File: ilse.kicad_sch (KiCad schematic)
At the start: 89 parts, among them J1 OUT, J2 EURO RACK POWER, J3 CV Inputs, J4 1V/Oct, J5 Gate, J6 Cutoff, J7 Filter In, Q1 BC560, Q2 BC560, Q3 BC560, Q4 BC550, Q5 BC550, Q6 BC550, SW1 Power Switch, SW2 LFO to Filter / Freq CV, SW3 Resonance L/H, U1 TL074, U2 TL074

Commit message: choose volume pot as linear type
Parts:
- H1, H2, H3, H4, LOGO1: now left out of the parts list
- RV7: value 100kA -> 100kB

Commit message: incorporates max's powersupply protection
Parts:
- removed SW1: Power Switch, chair:PVA2, symbol CHAIR:SW_Push_DPDT-Switch-PVA2
- added D3, D4: 1N5819, Diode_THT:D_DO-41_SOD81_P10.16mm_Horizontal, symbol Diode:1N5819
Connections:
- net VCC: now also C12.1, D3.1 (K)
- net VSS: now also C13.2, D4.2 (A)
- net at BT1.1 (+), J2.1 (+12V), J2.2 (+12V): now also D3.2 (A); no longer C12.1
- net at BT2.2 (-), J2.10 (-12V), J2.9 (-12V): now also D4.1 (K); no longer C13.2

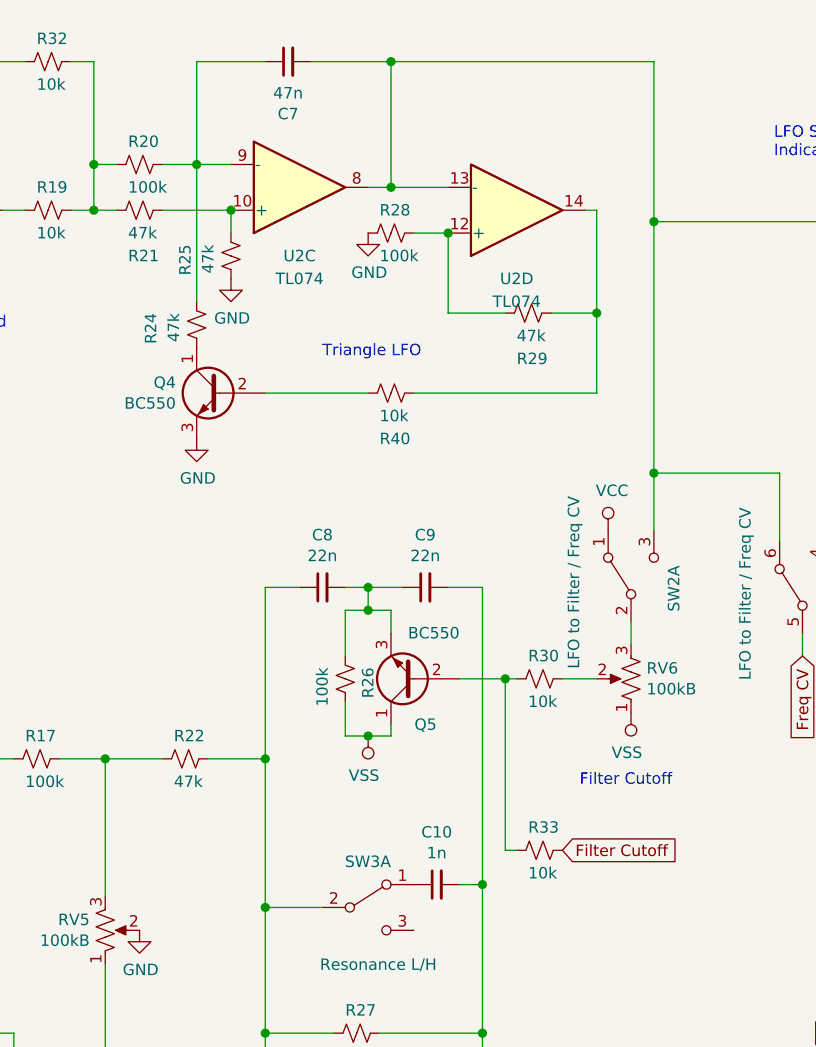
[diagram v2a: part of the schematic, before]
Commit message: removes filter distortion, cutoff modulation range is 0V - +10V, instead of -10V - +10V
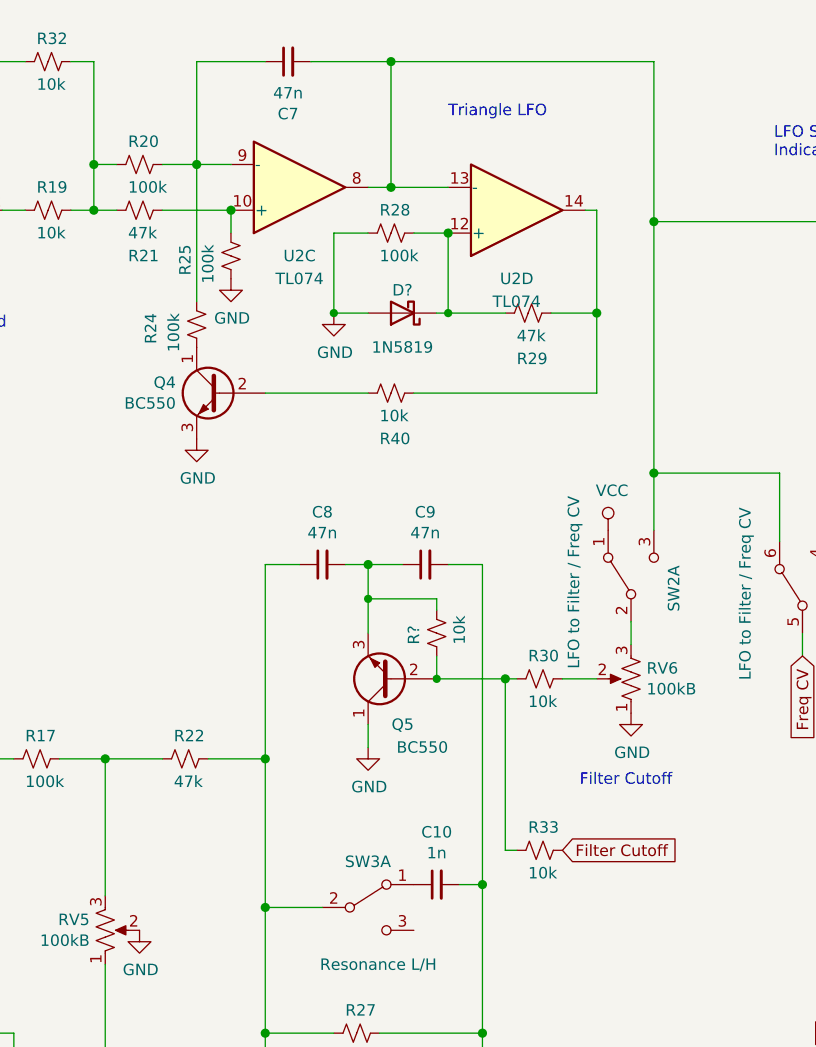
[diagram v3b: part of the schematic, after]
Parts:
- removed R26: 100k, Resistor_THT:R_Axial_DIN0207_L6.3mm_D2.5mm_P10.16mm_Horizontal, symbol ilse-rescue:R_Small_US-Device
- added D?: 1N5819, Diode_THT:D_DO-41_SOD81_P10.16mm_Horizontal, symbol Diode:1N5819
- added R?: 10k, Resistor_THT:R_Axial_DIN0207_L6.3mm_D2.5mm_P10.16mm_Horizontal, symbol ilse-rescue:R_Small_US-Device
- C8, C9: value 22n -> 47n
- R24, R25: value 47k -> 100k
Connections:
- net GND: now also Q5.1 (C), RV6.1, D?.2 (A)
- net VSS: no longer Q5.1 (C), RV6.1
- net at C8.2, C9.1, Q5.3 (E): now also R?.1
- net at Q5.2 (B), R30.2, R33.2: now also R?.2
- net at R28.1, R29.2, U2.12 (+): now also D?.1 (K)
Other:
- moved on the sheet: C8, C9, Q5

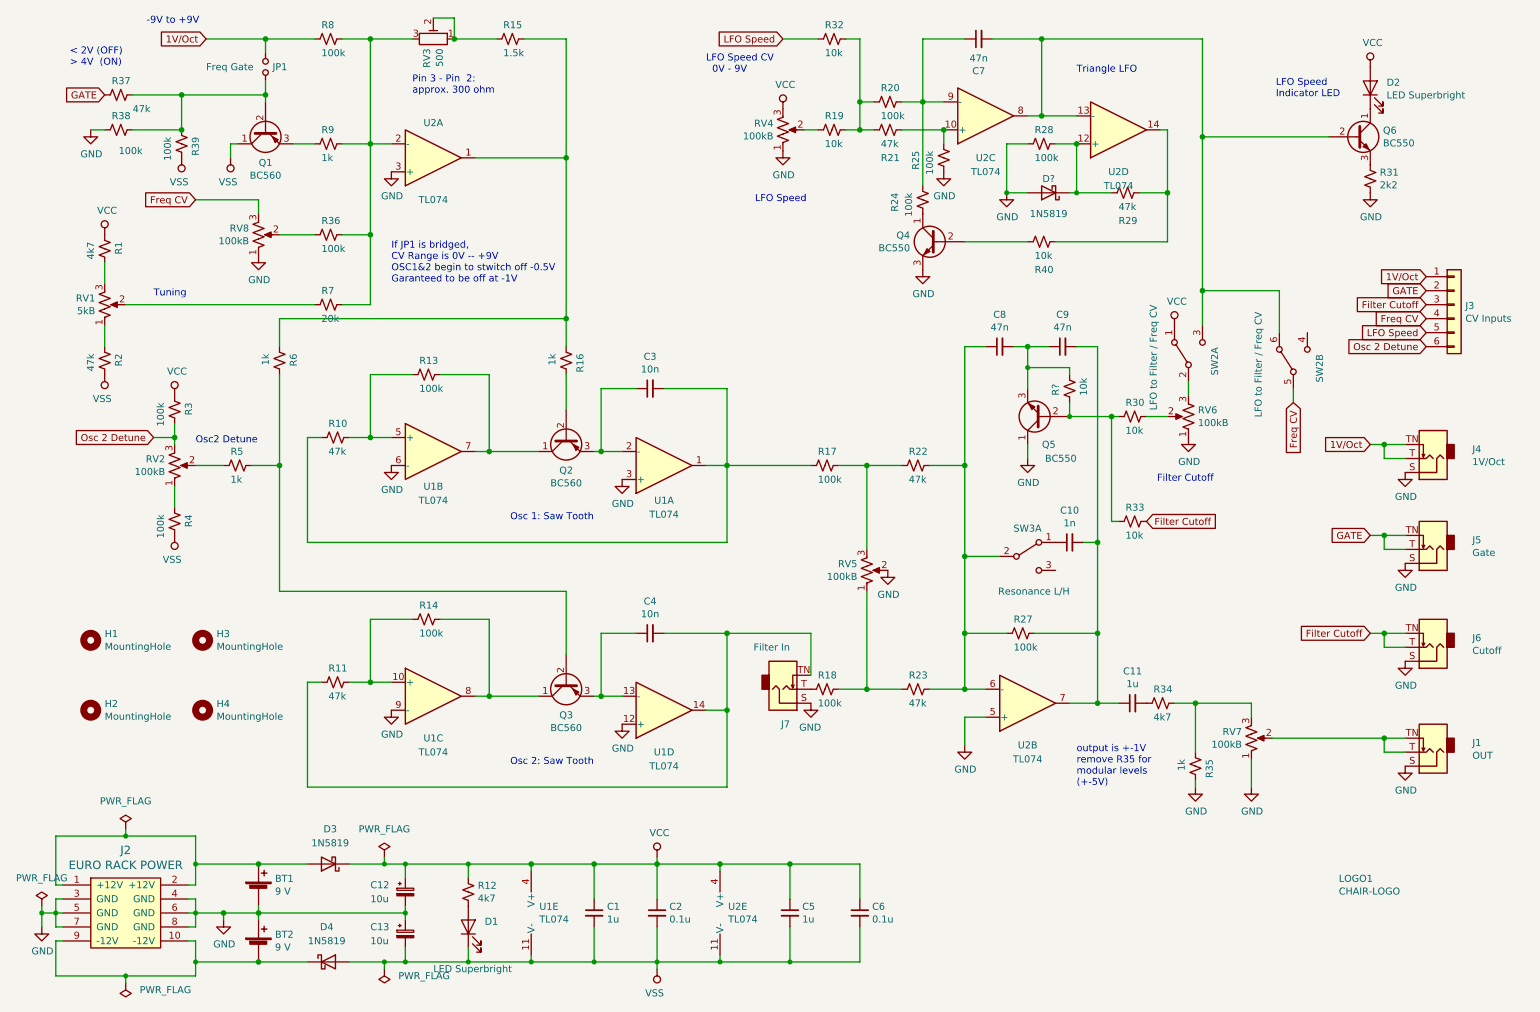
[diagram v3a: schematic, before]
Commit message: added hybrid lib
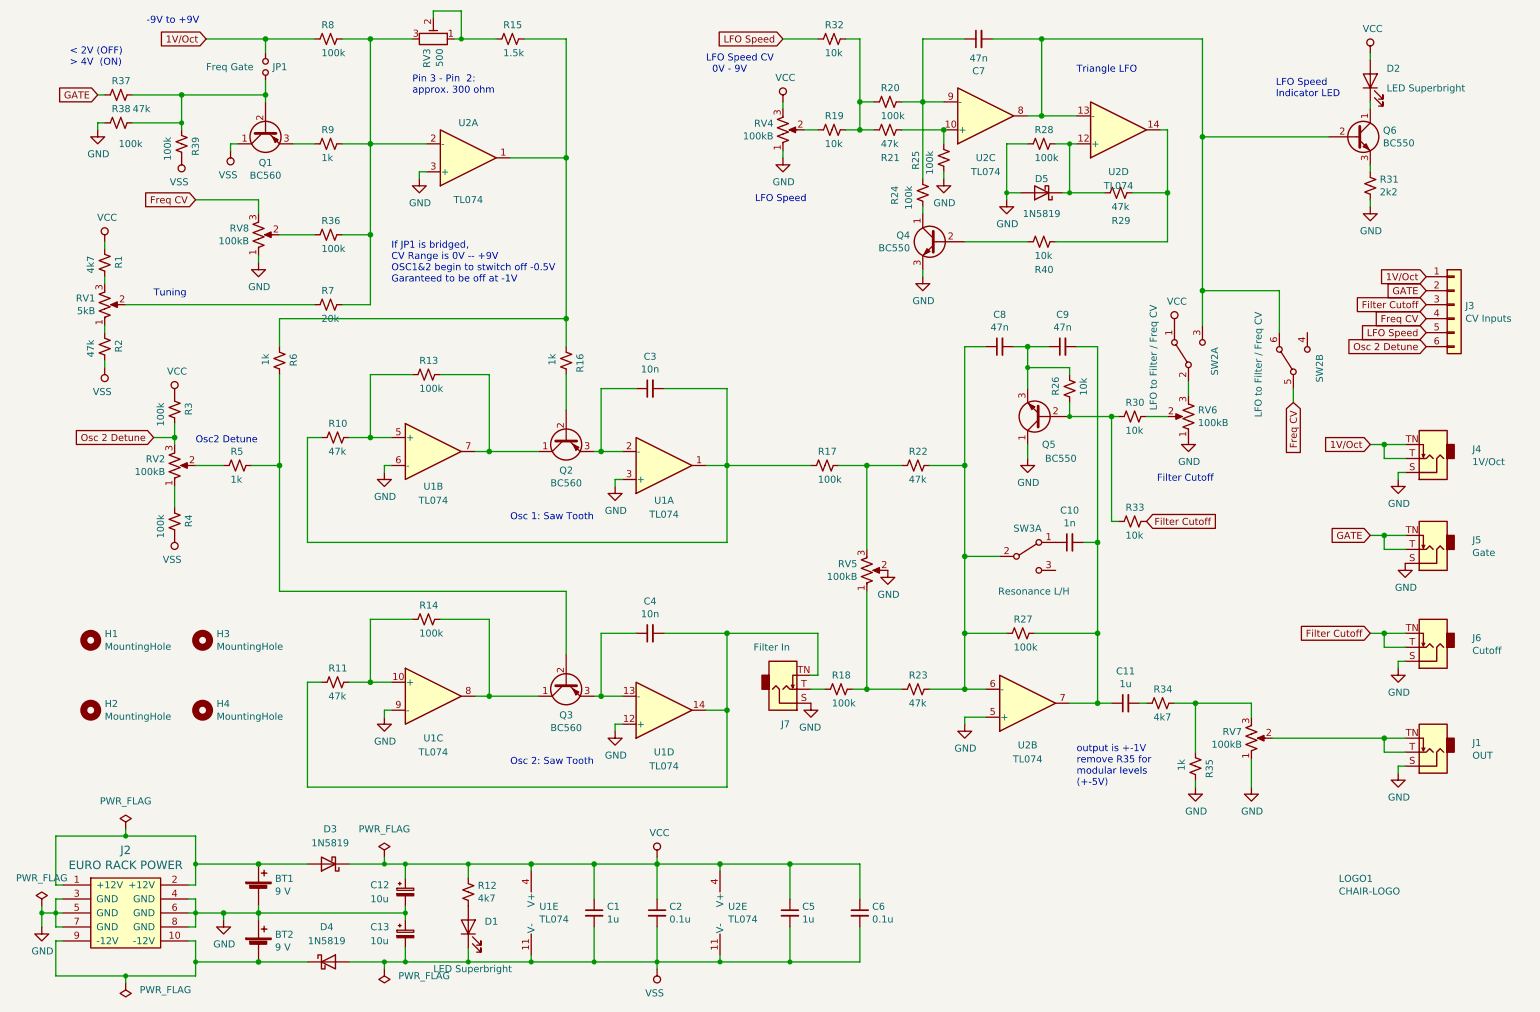
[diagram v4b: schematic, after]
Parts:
- R1, R12, R15, R19, R2, R20, R21, R23, R24, R25, R27, R28, R29, R3, R30, R31, R32, R33, R34, R35, R36, R37, R38, R39, R4, R40, R7, R8, R9: footprint Resistor_THT:R_Axial_DIN0207_L6.3mm_D2.5mm_P10.16mm_Horizontal -> hybrid:R (hybrid SMD-THT)
- R10, R11, R13, R14, R16, R17, R18, R22, R5, R6: footprint Resistor_THT:R_Axial_DIN0207_L6.3mm_D2.5mm_P2.54mm_Vertical -> hybrid:R (hybrid SMD-THT)
- R26: renamed from R?; footprint Resistor_THT:R_Axial_DIN0207_L6.3mm_D2.5mm_P10.16mm_Horizontal -> hybrid:R (hybrid SMD-THT)
- RV4, RV5, RV6, RV7, RV8: footprint chair:Potentiometer_Alps_RK09K_Single_Vertical -> CHAIR:Potentiometer_Alps_RK09K_Single_Vertical
- gave numbers to parts that had none: 1
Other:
- title: Ilse Rev1 -> Ilse
- moved on the sheet: C11, D2, D5, R1, R18, R2, R24, R29, R31, R38, U2A

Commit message: edits in schematic
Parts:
- BT1, BT2: footprint chair:Battery Connector -> Connector_PinHeader_2.54mm:PinHeader_1x02_P2.54mm_Vertical
- J1, J4, J5, J6, J7: footprint chair:Jack_3.5mm_QingPu_WQP-PJ398SM_Vertical_CircularHoles -> CHAIR:Jack_3.5mm_QingPu_WQP-WQP518MA
- J2: footprint 4ms-footprints:Euro_Header_10-pin_TH -> CHAIR:Euro_Header_10-pin_TH
- LOGO1: footprint chair:CHAIR -> CHAIR:CHAIR_logo_silkscreen
- RV1, RV2: footprint chair:Potentiometer_Alps_RK09K_Single_Vertical -> CHAIR:Potentiometer_Alps_RK09K_Single_Vertical
- SW2, SW3: footprint chair:PVA2 -> CHAIR:Switch_DPDT_PVA2
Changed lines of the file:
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@@
       (effects (font (size 1.27 1.27)) (justify right))
     )
-    (property "Footprint" "chair:Jack_3.5mm_QingPu_WQP-PJ398SM_Vertical_CircularHoles" (id 2) (at 270.51 149.86 0)
+    (property "Footprint" "CHAIR:Jack_3.5mm_QingPu_WQP-WQP518MA" (id 2) (at 270.51 149.86 0)
       (effects (font (size 1.27 1.27)) hide)
     )
@@
       (effects (font (size 1.27 1.27)) (justify right))
     )
-    (property "Footprint" "chair:Potentiometer_Alps_RK09K_Single_Vertical" (id 2) (at 29.21 68.58 0)
+    (property "Footprint" "CHAIR:Potentiometer_Alps_RK09K_Single_Vertical" (id 2) (at 29.21 68.58 0)
       (effects (font (size 1.27 1.27)) hide)
     )
@@
       (effects (font (size 1.27 1.27)) (justify right))
     )
-    (property "Footprint" "chair:Potentiometer_Alps_RK09K_Single_Vertical" (id 2) (at 41.91 97.79 0)
+    (property "Footprint" "CHAIR:Potentiometer_Alps_RK09K_Single_Vertical" (id 2) (at 41.91 97.79 0)
       (effects (font (size 1.27 1.27)) hide)
     )
@@
       (effects (font (size 1.27 1.27)) (justify right))
     )
-    (property "Footprint" "chair:PVA2" (id 2) (at 245.11 78.74 0)
+    (property "Footprint" "CHAIR:Switch_DPDT_PVA2" (id 2) (at 245.11 78.74 0)
       (effects (font (size 1.27 1.27)) hide)
     )
@@
       (effects (font (size 1.27 1.27)) (justify right))
     )
-    (property "Footprint" "chair:PVA2" (id 2) (at 196.85 114.3 0)
+    (property "Footprint" "CHAIR:Switch_DPDT_PVA2" (id 2) (at 196.85 114.3 0)
       (effects (font (size 1.27 1.27)) hide)
     )
@@
       (effects (font (size 1.27 1.27)) (justify right))
     )
-    (property "Footprint" "chair:PVA2" (id 2) (at 226.06 77.47 0)
+    (property "Footprint" "CHAIR:Switch_DPDT_PVA2" (id 2) (at 226.06 77.47 0)
       (effects (font (size 1.27 1.27)) hide)
     )
@@
       (effects (font (size 1.27 1.27)) (justify right))
     )
-    (property "Footprint" "chair:Jack_3.5mm_QingPu_WQP-PJ398SM_Vertical_CircularHoles" (id 2) (at 152.4 138.43 0)
+    (property "Footprint" "CHAIR:Jack_3.5mm_QingPu_WQP-WQP518MA" (id 2) (at 152.4 138.43 0)
       (effects (font (size 1.27 1.27)) hide)
     )
@@
       (effects (font (size 1.27 1.27)) (justify right))
     )
-    (property "Footprint" "chair:Jack_3.5mm_QingPu_WQP-PJ398SM_Vertical_CircularHoles" (id 2) (at 270.51 96.52 0)
+    (property "Footprint" "CHAIR:Jack_3.5mm_QingPu_WQP-WQP518MA" (id 2) (at 270.51 96.52 0)
       (effects (font (size 1.27 1.27)) hide)
     )
@@
       (effects (font (size 1.27 1.27)) (justify right))
     )
-    (property "Footprint" "chair:Jack_3.5mm_QingPu_WQP-PJ398SM_Vertical_CircularHoles" (id 2) (at 270.51 113.03 0)
+    (property "Footprint" "CHAIR:Jack_3.5mm_QingPu_WQP-WQP518MA" (id 2) (at 270.51 113.03 0)
       (effects (font (size 1.27 1.27)) hide)
     )
@@
       (effects (font (size 1.27 1.27)) (justify right))
     )
-    (property "Footprint" "chair:Jack_3.5mm_QingPu_WQP-PJ398SM_Vertical_CircularHoles" (id 2) (at 270.51 130.81 0)
+    (property "Footprint" "CHAIR:Jack_3.5mm_QingPu_WQP-WQP518MA" (id 2) (at 270.51 130.81 0)
       (effects (font (size 1.27 1.27)) hide)
     )
@@
       (effects (font (size 1.27 1.27)) (justify left))
     )
-    (property "Footprint" "chair:CHAIR" (id 2) (at 252.73 173.99 0)
+    (property "Footprint" "CHAIR:CHAIR_logo_silkscreen" (id 2) (at 252.73 173.99 0)
       (effects (font (size 1.27 1.27)) hide)
     )
@@
       (effects (font (size 1.27 1.27)) (justify left))
     )
-    (property "Footprint" "chair:Battery Connector" (id 2) (at 57.15 173.736 90)
+    (property "Footprint" "Connector_PinHeader_2.54mm:PinHeader_1x02_P2.54mm_Vertical" (id 2) (at 57.15 173.736 90)
       (effects (font (size 1.27 1.27)) hide)
     )
@@
       (effects (font (size 1.27 1.27)) (justify left))
     )
-    (property "Footprint" "chair:Battery Connector" (id 2) (at 57.15 183.896 90)
+    (property "Footprint" "Connector_PinHeader_2.54mm:PinHeader_1x02_P2.54mm_Vertical" (id 2) (at 57.15 183.896 90)
       (effects (font (size 1.27 1.27)) hide)
     )
@@
       (effects (font (size 1.524 1.524)))
     )
-    (property "Footprint" "4ms-footprints:Euro_Header_10-pin_TH" (id 2) (at 33.02 179.07 0)
+    (property "Footprint" "CHAIR:Euro_Header_10-pin_TH" (id 2) (at 33.02 179.07 0)
       (effects (font (size 1.524 1.524)) hide)
     )
@@
     )
     (path "/1859c414-a0ba-4381-8fb3-2425d19b7e92"
-      (reference "BT1") (unit 1) (value "9 V") (footprint "chair:Battery Connector")
+      (reference "BT1") (unit 1) (value "9 V") (footprint "Connector_PinHeader_2.54mm:PinHeader_1x02_P2.54mm_Vertical")
     )
     (path "/2b774f6e-fa63-4a95-9950-c9cc2ceace8e"
-      (reference "BT2") (unit 1) (value "9 V") (footprint "chair:Battery Connector")
+      (reference "BT2") (unit 1) (value "9 V") (footprint "Connector_PinHeader_2.54mm:PinHeader_1x02_P2.54mm_Vertical")
     )
     (path "/00000000-0000-0000-0000-00005db62548"
@@
     )
     (path "/00000000-0000-0000-0000-00005da6e8b4"
-      (reference "J1") (unit 1) (value "OUT") (footprint "chair:Jack_3.5mm_QingPu_WQP-PJ398SM_Vertical_CircularHoles")
+      (reference "J1") (unit 1) (value "OUT") (footprint "CHAIR:Jack_3.5mm_QingPu_WQP-WQP518MA")
     )
     (path "/f65734c0-1d2e-4314-893e-1906a6e28793"
-      (reference "J2") (unit 1) (value "EURO RACK POWER") (footprint "4ms-footprints:Euro_Header_10-pin_TH")
+      (reference "J2") (unit 1) (value "EURO RACK POWER") (footprint "CHAIR:Euro_Header_10-pin_TH")
     )
     (path "/00000000-0000-0000-0000-00005db87452"
@@
     )
     (path "/00000000-0000-0000-0000-00005df0fdaf"
-      (reference "J4") (unit 1) (value "1V/Oct") (footprint "chair:Jack_3.5mm_QingPu_WQP-PJ398SM_Vertical_CircularHoles")
+      (reference "J4") (unit 1) (value "1V/Oct") (footprint "CHAIR:Jack_3.5mm_QingPu_WQP-WQP518MA")
     )
     (path "/00000000-0000-0000-0000-00005df14111"
-      (reference "J5") (unit 1) (value "Gate") (footprint "chair:Jack_3.5mm_QingPu_WQP-PJ398SM_Vertical_CircularHoles")
+      (reference "J5") (unit 1) (value "Gate") (footprint "CHAIR:Jack_3.5mm_QingPu_WQP-WQP518MA")
     )
     (path "/00000000-0000-0000-0000-00005df14ed1"
-      (reference "J6") (unit 1) (value "Cutoff") (footprint "chair:Jack_3.5mm_QingPu_WQP-PJ398SM_Vertical_CircularHoles")
+      (reference "J6") (unit 1) (value "Cutoff") (footprint "CHAIR:Jack_3.5mm_QingPu_WQP-WQP518MA")
     )
     (path "/00000000-0000-0000-0000-00005dbe8685"
-      (reference "J7") (unit 1) (value "Filter In") (footprint "chair:Jack_3.5mm_QingPu_WQP-PJ398SM_Vertical_CircularHoles")
+      (reference "J7") (unit 1) (value "Filter In") (footprint "CHAIR:Jack_3.5mm_QingPu_WQP-WQP518MA")
     )
     (path "/00000000-0000-0000-0000-00005dbd1563"
@@
     )
     (path "/00000000-0000-0000-0000-00005df4867e"
-      (reference "LOGO1") (unit 1) (value "CHAIR-LOGO") (footprint "chair:CHAIR")
+      (reference "LOGO1") (unit 1) (value "CHAIR-LOGO") (footprint "CHAIR:CHAIR_logo_silkscreen")
     )
     (path "/00000000-0000-0000-0000-00005dbc3bae"
@@
     )
     (path "/00000000-0000-0000-0000-00005db3b27c"
-      (reference "RV1") (unit 1) (value "5kB") (footprint "chair:Potentiometer_Alps_RK09K_Single_Vertical")
+      (reference "RV1") (unit 1) (value "5kB") (footprint "CHAIR:Potentiometer_Alps_RK09K_Single_Vertical")
     )
     (path "/00000000-0000-0000-0000-00005db66e8d"
-      (reference "RV2") (unit 1) (value "100kB") (footprint "chair:Potentiometer_Alps_RK09K_Single_Vertical")
+      (reference "RV2") (unit 1) (value "100kB") (footprint "CHAIR:Potentiometer_Alps_RK09K_Single_Vertical")
     )
     (path "/00000000-0000-0000-0000-00005db4a068"
@@
     )
     (path "/00000000-0000-0000-0000-00005dba5cfc"
-      (reference "SW2") (unit 1) (value "LFO to Filter / Freq CV") (footprint "chair:PVA2")
+      (reference "SW2") (unit 1) (value "LFO to Filter / Freq CV") (footprint "CHAIR:Switch_DPDT_PVA2")
     )
     (path "/00000000-0000-0000-0000-00005db7961b"
-      (reference "SW2") (unit 2) (value "LFO to Filter / Freq CV") (footprint "chair:PVA2")
+      (reference "SW2") (unit 2) (value "LFO to Filter / Freq CV") (footprint "CHAIR:Switch_DPDT_PVA2")
     )
     (path "/00000000-0000-0000-0000-00005db8960d"
-      (reference "SW3") (unit 1) (value "Resonance L/H") (footprint "chair:PVA2")
+      (reference "SW3") (unit 1) (value "Resonance L/H") (footprint "CHAIR:Switch_DPDT_PVA2")
     )
     (path "/00000000-0000-0000-0000-00005da11bf4"
